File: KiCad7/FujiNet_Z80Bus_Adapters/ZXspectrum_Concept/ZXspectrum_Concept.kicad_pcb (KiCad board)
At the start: 2 copper layers, 200 x 130 mm, 39 parts, among them IC1 74HC165N, IC10 74595N, IC2 74HC244N, IC3 74HC165N, IC4 74595N, IC5 74HC165N, IC6 74595N, IC7 74HC32N, IC8 74HC165N, IC9 74595N, J7 DIAG-HOST_SYSTEM_BUS, U1 FREENOVE_ESP32-WROVER-DEV

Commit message: KiCad ZXspectrum concept
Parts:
- moved EX_SPI1 149.4 mm to (48.0, 125.8), turned to 0 degrees
- moved Z80_control.in1 115.7 mm to (127.5, 119.9), turned to -90 degrees
- moved D3 106.2 mm to (224.0, 140.8)
- moved D4 106.2 mm to (224.0, 145.0)
- moved D2 106.2 mm to (224.0, 136.7)
- moved U1 96.5 mm to (213.9, 137.0)
- moved D1 96.1 mm to (216.0, 142.0)
- moved R2 95.6 mm to (219.1, 129.0)
- moved R1 94.1 mm to (229.3, 132.5)
- moved GLUE2 89.9 mm to (104.5, 43.5), turned to 90 degrees
- moved R3 89.4 mm to (75.1, 147.5), turned to 180 degrees
- moved IC1 82.9 mm to (74.9, 136.2)
- moved Local_addr-l.in1 81.1 mm to (221.5, 55.0), turned to -90 degrees
- moved Local_addr-h.in1 69.7 mm to (221.5, 38.4), turned to -90 degrees
- moved GLUE1 58.2 mm to (104.5, 135.5), turned to 90 degrees
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- renumbered IC2 to Control_selection1, IC6 to ESP_Control1, IC7 to IC1, IC8 to Local_addr-h.in1, IC5 to Local_addr-l.in1, IC10 to Local_addr_h.out1, IC9 to Local_addr_l.out1, IC1 to Local_data.in1, IC4 to Local_data.out1, IC3 to Z80_control.in1
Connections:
- GLUE1 pad 22: /CORE/Z80_HARDLOCK -> /CACHE connector/Z80_HARDLOCK
- GLUE2 pad 13: /GLUE connector/CACHE_CONTROL.DATASTATUS+PERM_Z80_IORQ -> /CACHE connector/CACHE_CONTROL.DATASTATUS+PERM_Z80_IORQ
- GLUE2 pad 14: /GLUE connector/CACHE_CONTROL.A16 -> /CACHE connector/CACHE_CONTROL.A16
- GLUE2 pad 15: /GLUE connector/CACHE_CONTROL.WE -> /CACHE connector/CACHE_CONTROL.WE
- GLUE2 pad 16: /GLUE connector/CACHE_CONTROL.OE -> /CACHE connector/CACHE_CONTROL.OE
- GLUE2 pad 17: /GLUE connector/CACHE_CONTROL.CS -> /CACHE connector/CACHE_CONTROL.CS
- RIO2 pad 2: /RIO connector/RIO_CONTROL.A16 -> /GLUE connector/RIO_CONTROL.A16
- RIO2 pad 3: /RIO connector/RIO_CONTROL.A15 -> /GLUE connector/RIO_CONTROL.A15
- RIO2 pad 4: /RIO connector/RIO_CONTROL.A14 -> /GLUE connector/RIO_CONTROL.A14
- RIO2 pad 5: /RIO connector/RIO_CONTROL.WE -> /GLUE connector/RIO_CONTROL.WE
- RIO2 pad 6: /RIO connector/RIO_CONTROL.CE -> /GLUE connector/RIO_CONTROL.CE
- RIO2 pad 7: /RIO connector/RIO_CONTROL.OE -> /GLUE connector/RIO_CONTROL.OE
- RIO2 pad 8: /RIO connector/RIO_CONTROL.ROM_RDY -> /GLUE connector/RIO_CONTROL.ROM_RDY
- U1 pad 4: /CORE/Z80_HARDLOCK -> /CACHE connector/Z80_HARDLOCK

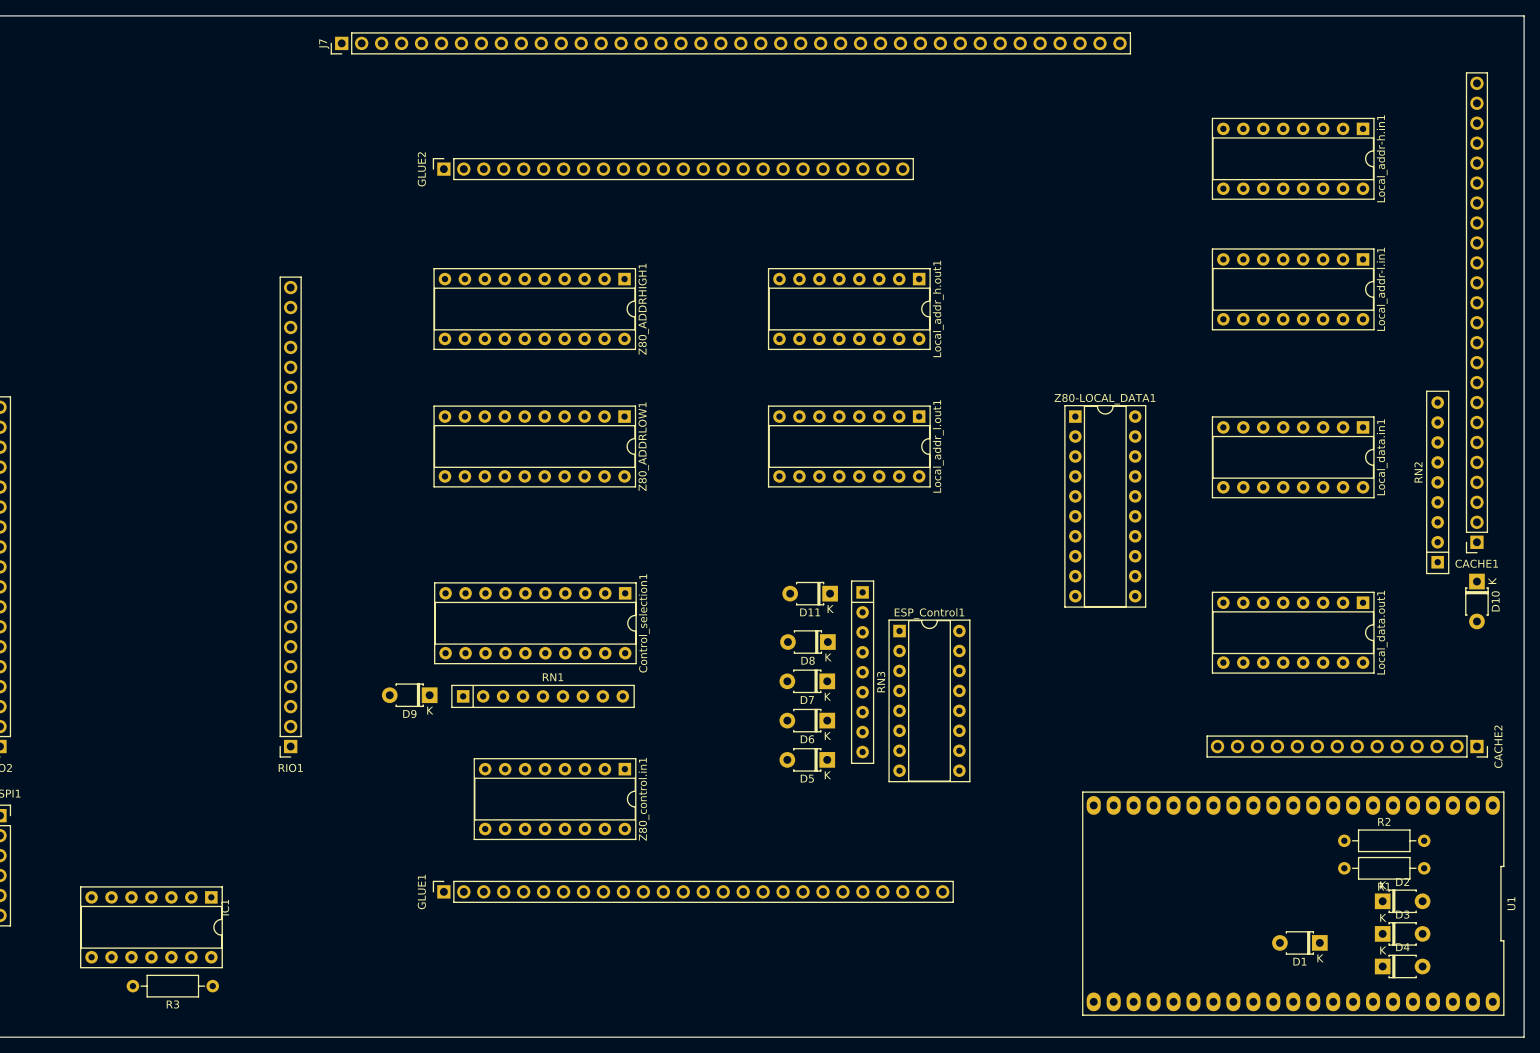
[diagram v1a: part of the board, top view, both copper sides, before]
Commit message: KiCad Another attempt to route concept adapter
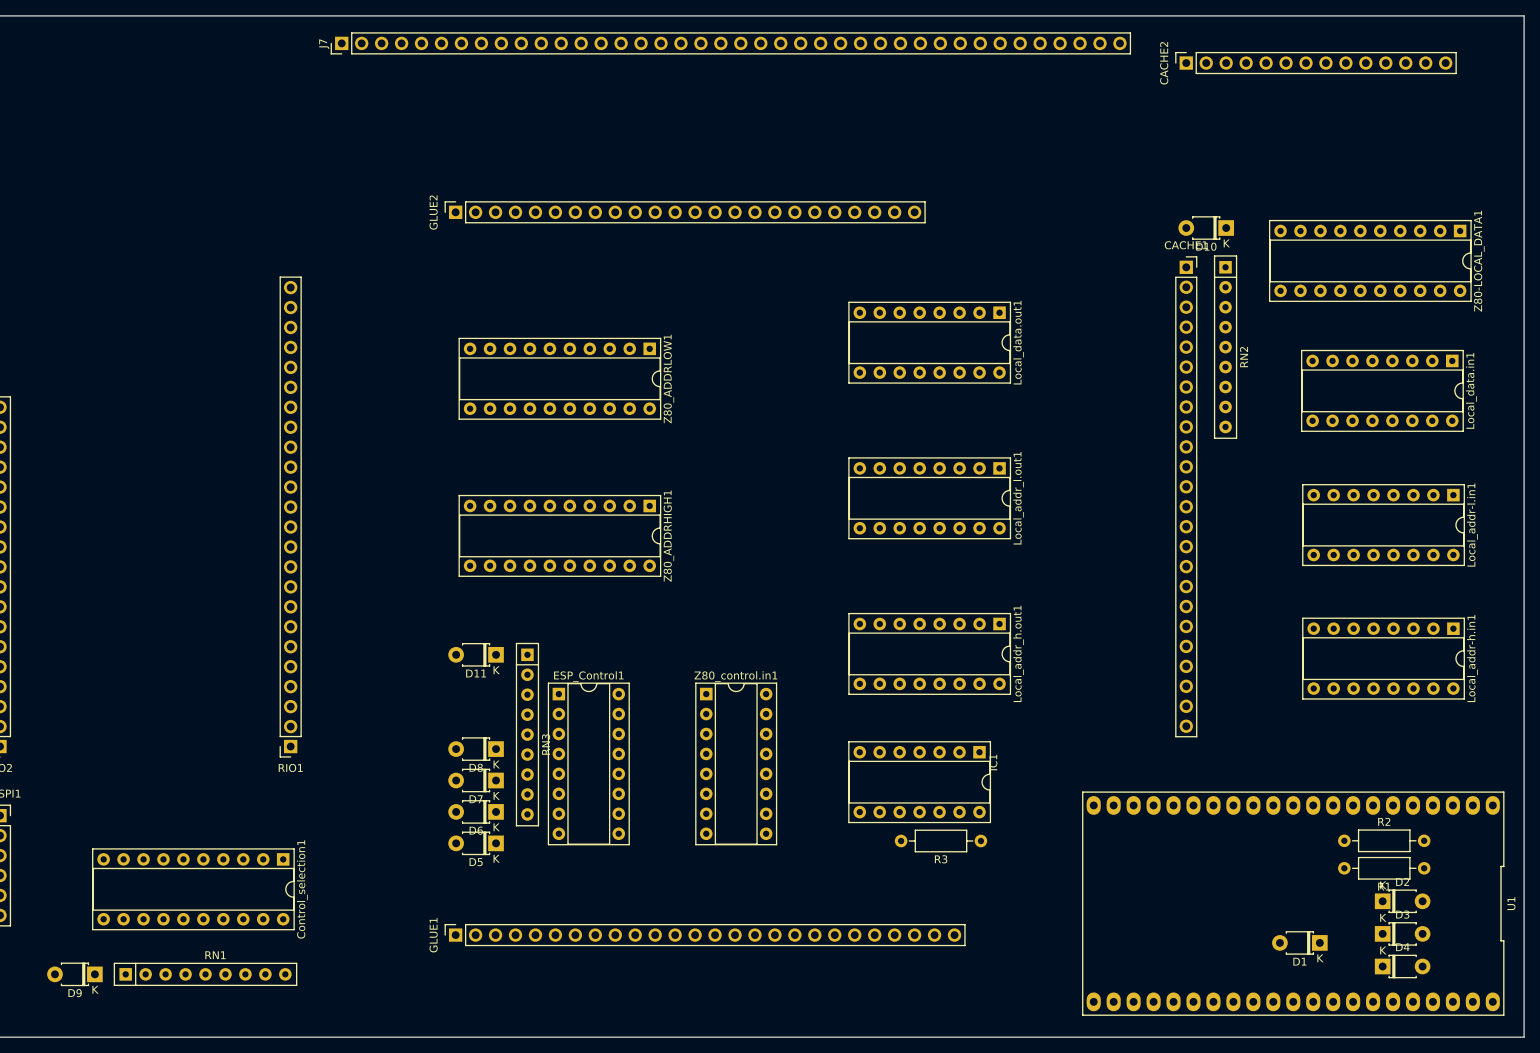
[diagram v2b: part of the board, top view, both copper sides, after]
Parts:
- moved IC1 99.5 mm to (172.7, 117.7)
- moved R3 99.5 mm to (172.9, 129.0)
- moved CACHE2 94.5 mm to (199.0, 30.0), turned to 90 degrees
- moved Local_addr-h.in1 64.7 mm to (233.0, 102.0)
- moved Local_data.out1 59.2 mm to (175.2, 61.8)
- moved RN1 55.7 mm to (64.0, 146.0)
- moved D9 55.5 mm to (60.1, 146.0)
- moved D10 55.2 mm to (204.1, 51.0), turned to 180 degrees
- moved Control_selection1 55.2 mm to (84.0, 131.4)
- moved Z80-LOCAL_DATA1 54.4 mm to (233.9, 51.4), turned to -90 degrees
- moved CACHE1 50.9 mm to (199.0, 56.0), turned to 0 degrees
- moved RN2 46.2 mm to (204.0, 56.0), turned to -90 degrees
- moved Local_addr_h.out1 45.1 mm to (175.2, 101.4)
- moved D8 44.4 mm to (111.1, 117.3)
- moved ESP_Control1 44.1 mm to (119.1, 110.3)
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
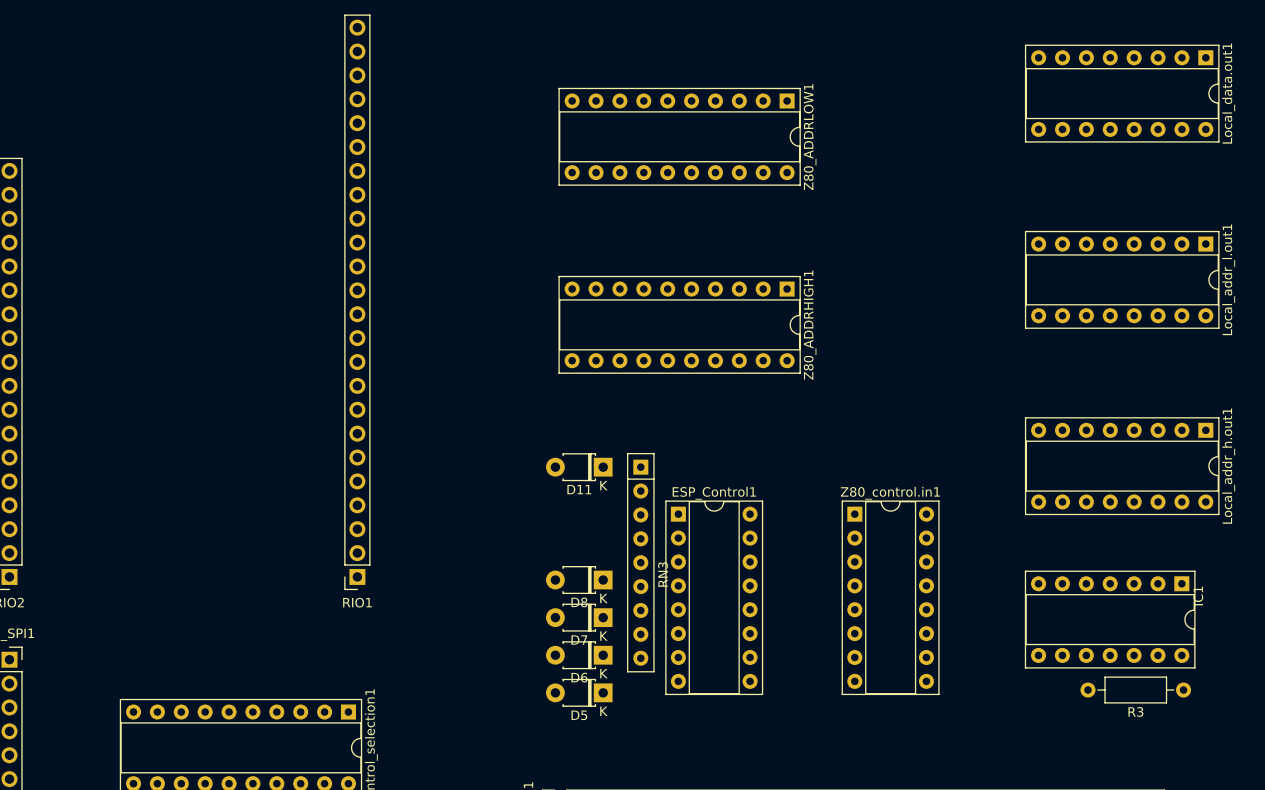
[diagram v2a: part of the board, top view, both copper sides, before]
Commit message: Kicad concept adapter still wont route
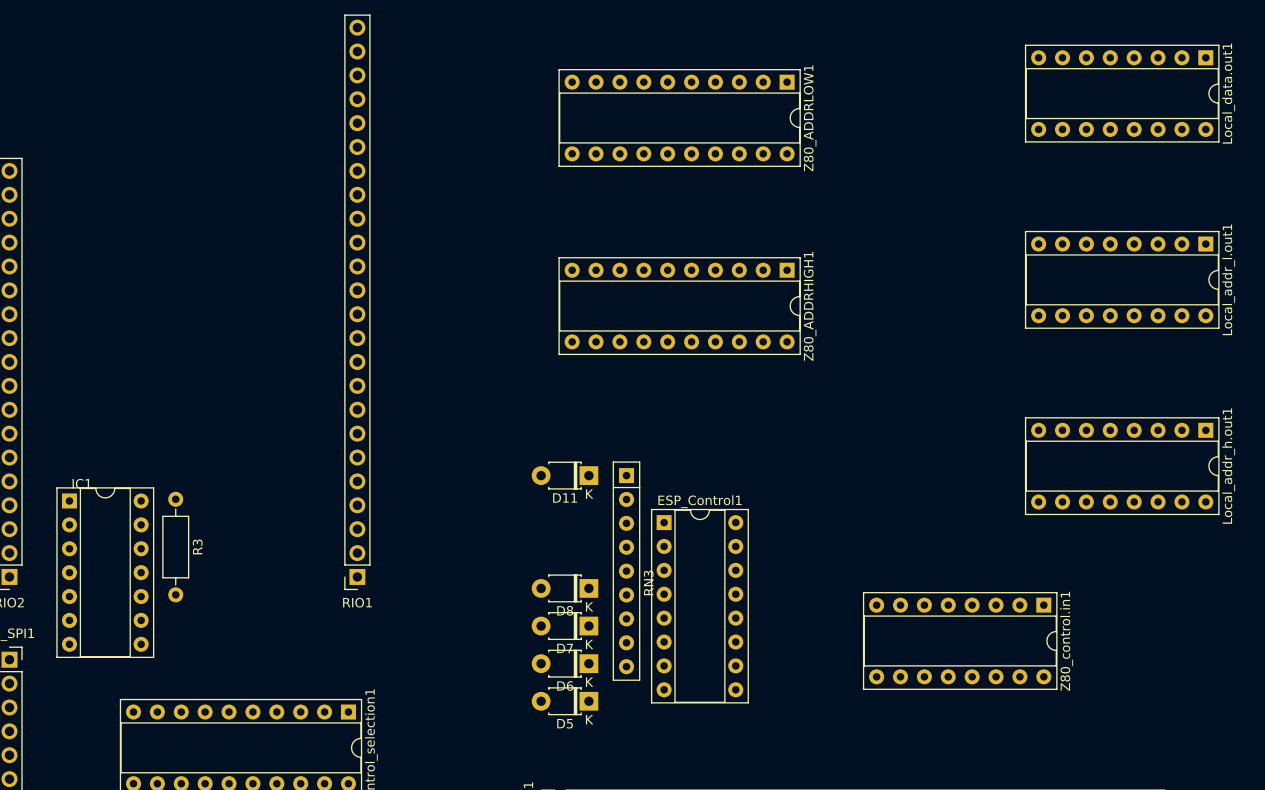
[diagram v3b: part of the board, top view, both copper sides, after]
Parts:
- moved IC1 118.6 mm to (54.4, 108.9), turned to 0 degrees
- moved R3 109.1 mm to (65.7, 108.7), turned to -90 degrees
- moved Z80_control.in1 22.3 mm to (158.0, 120.0), turned to -90 degrees
- moved Z80_ADDRHIGH1 2.00 mm to (130.7, 84.4)
- moved Z80_ADDRLOW1 2.00 mm to (130.7, 64.4)
- moved D5 1.76 mm to (109.6, 130.2)
- moved D11 1.76 mm to (109.6, 106.2)
- moved D6 1.76 mm to (109.6, 126.2)
- moved D7 1.76 mm to (109.6, 122.2)
- moved D8 1.76 mm to (109.6, 118.2)
- moved ESP_Control1 1.76 mm to (117.6, 111.2)
- moved RN3 1.76 mm to (113.6, 106.2)

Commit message: KiCad Revision 2 of zxspectrum concept adapter
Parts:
- added CACHE1: Conn_01x24_Socket, Connector_PinSocket_2.54mm:PinSocket_1x24_P2.54mm_Vertical, F.Cu at (344.6, 125.0)
- added CACHE2: Conn_01x14_Socket, Connector_PinSocket_2.54mm:PinSocket_1x14_P2.54mm_Vertical, F.Cu at (318.6, 125.0)
- added D1: 1N4148, Diode_THT:D_T-1_P5.08mm_Horizontal, F.Cu at (484.0, 166.5)
- added D2: 1N4148, Diode_THT:D_T-1_P5.08mm_Horizontal, F.Cu at (489.3, 174.5)
- added D3: 1N4148, Diode_THT:D_T-1_P5.08mm_Horizontal, F.Cu at (485.1, 174.5)
- added D4: 1N4148, Diode_THT:D_T-1_P5.08mm_Horizontal, F.Cu at (481.0, 174.5)
- added EX_SPI1: PinSocket_2.54mm, Connector_PinSocket_2.54mm:PinSocket_1x06_P2.54mm_Vertical, F.Cu at (508.0, 139.0)
- added J7: DIAG-HOST_SYSTEM_BUS, Connector_PinHeader_2.54mm:PinHeader_1x40_P2.54mm_Vertical, F.Cu at (360.5, 69.0)
- added R1: 22K, Resistor_THT:R_Axial_DIN0207_L6.3mm_D2.5mm_P10.16mm_Horizontal, F.Cu at (493.5, 179.8)
- added R2: 22K, Resistor_THT:R_Axial_DIN0207_L6.3mm_D2.5mm_P10.16mm_Horizontal, F.Cu at (497.0, 169.7)
- added RIO1: Conn_01x24_Socket, Connector_PinSocket_2.54mm:PinSocket_1x24_P2.54mm_Vertical, F.Cu at (502.6, 88.0)
- added RIO2: Conn_01x18_Socket, Connector_PinSocket_2.54mm:PinSocket_1x18_P2.54mm_Vertical, F.Cu at (502.6, 125.0)
- added U1: FREENOVE_ESP32-WROVER-DEV, esp32-wrover:FREENOVE_ESP32-WROVER-DEV, F.Cu at (489.0, 164.4)
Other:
- board text added: "SPI BUS"

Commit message: KiCad Adapter Concept v2 pcb draft layout
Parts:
- removed the CACHE1 at (344.6, 125.0)
- removed the CACHE2 at (318.6, 125.0)
- removed the D1 at (484.0, 166.5)
- removed the D2 at (489.3, 174.5)
- removed the D3 at (485.1, 174.5)
- removed the D4 at (481.0, 174.5)
- removed the EX_SPI1 at (508.0, 139.0)
- removed the J7 at (360.5, 69.0)
- removed the R1 at (493.5, 179.8)
- removed the R2 at (497.0, 169.7)
- removed the RIO1 at (502.6, 88.0)
- removed the RIO2 at (502.6, 125.0)
- removed the U1 at (489.0, 164.4)
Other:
- board text removed: "SPI BUS"
